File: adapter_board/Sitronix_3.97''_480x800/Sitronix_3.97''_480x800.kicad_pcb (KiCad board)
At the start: 2 copper layers, 32.5 x 54.9 mm, 6 parts, among them J1 ESP32-S3-LCD-EV-BOARD_SUB_LCD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, J2 Conn_02x26_Counter_Clockwise, J3 Conn_01x03, J4 Conn_01x02

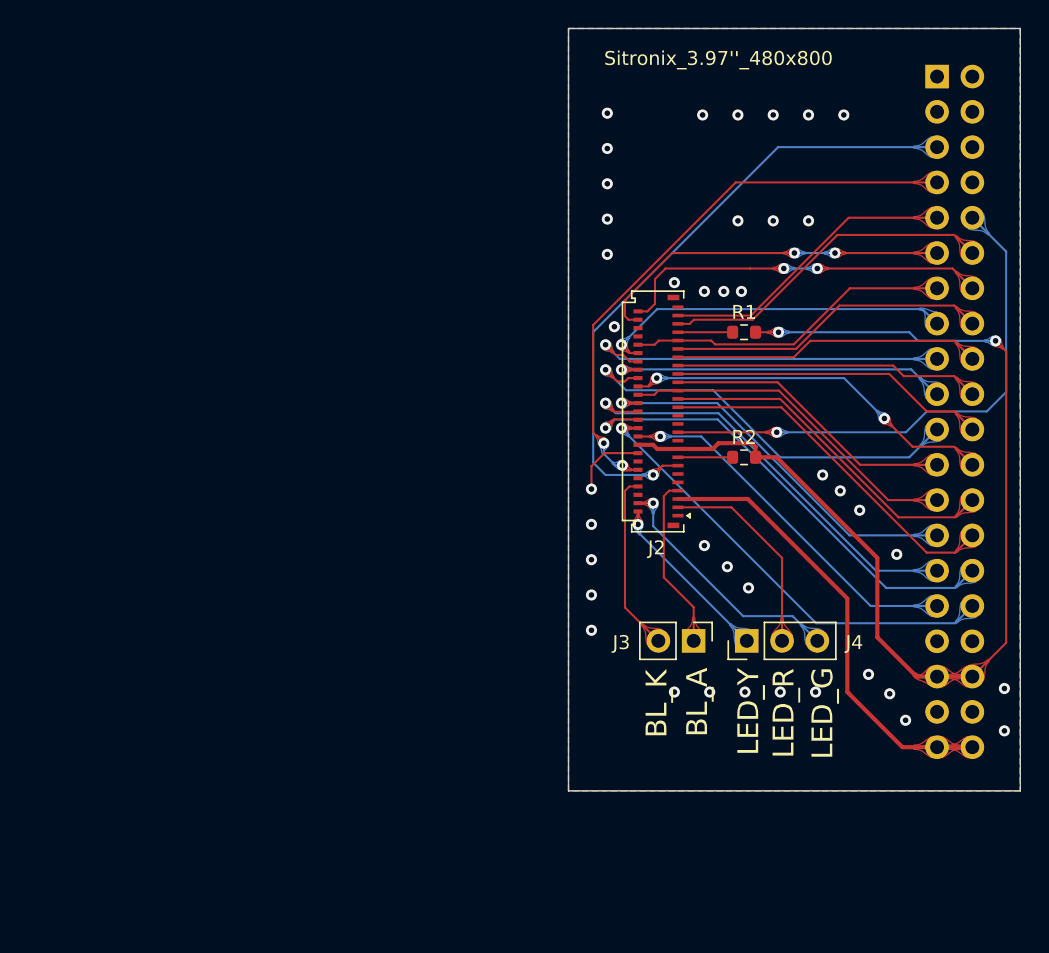
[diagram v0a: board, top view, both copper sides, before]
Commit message: adapter_board.sitronix_3.97''_800x480: modify
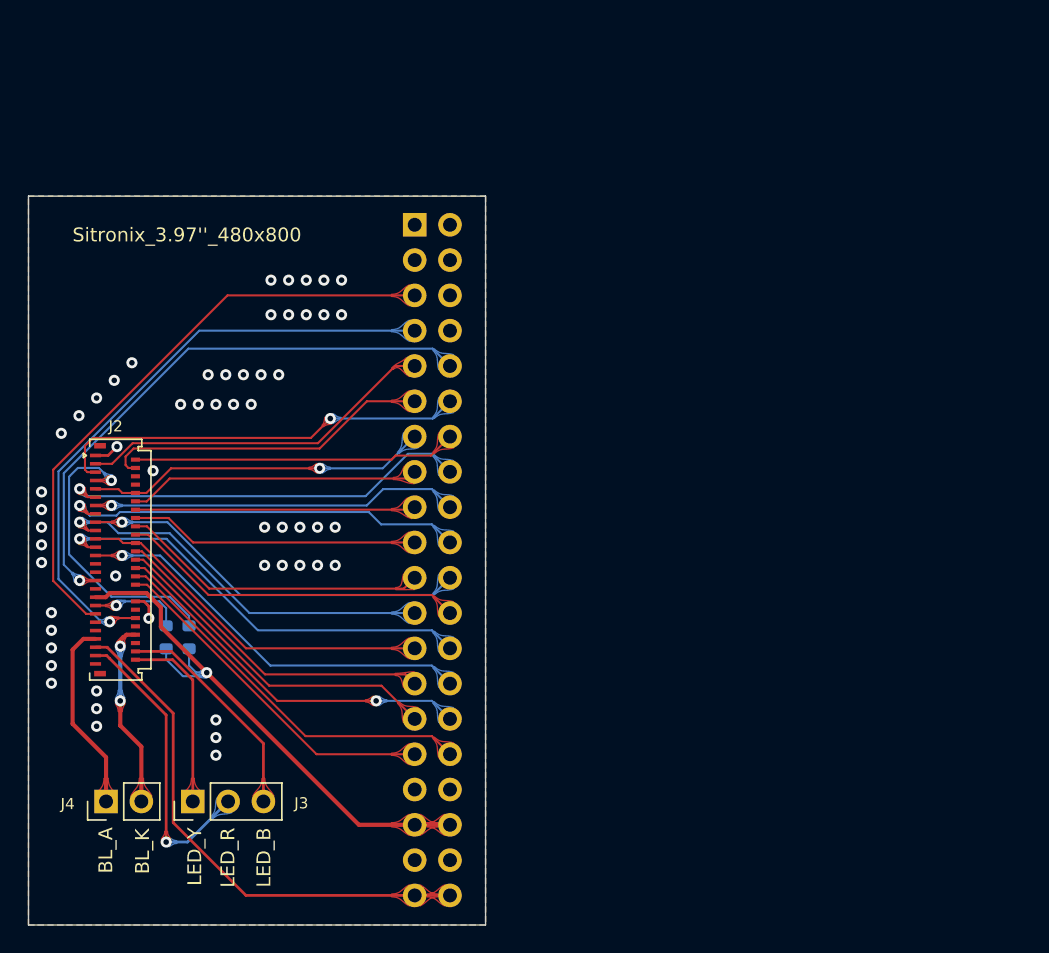
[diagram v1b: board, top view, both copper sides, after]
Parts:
- R1, R2: moved to B.Cu
- moved R1 45.6 mm to (46.7, 103.6), turned to -90 degrees
- moved J4 43.8 mm to (40.8, 115.4), turned to 90 degrees
- moved R2 43.6 mm to (45.1, 103.6), turned to -90 degrees
- moved J3 41.5 mm to (47.0, 115.4)
- moved J2 40.5 mm to (41.4, 98.0), turned to 0 degrees
- moved J1 39.1 mm to (63.0, 73.9)
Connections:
- J2 pad 10: unconnected-(J2-Pad10) -> /LCD_B3
- J2 pad 11: /GND -> /LCD_B4
- J2 pad 12: /TP_SCL -> /LCD_B5
- J2 pad 13: /TP_SDA -> /LCD_B6
- J2 pad 14: unconnected-(J2-Pad14) -> /LCD_B7
- J2 pad 15: Net-(J2-Pad15) -> /LCD_G2
- J2 pad 16: /GND -> /LCD_G3
- J2 pad 17: /VCC3.3V -> /LCD_G4
- J2 pad 18: /VCC3.3V -> /LCD_G5
- J2 pad 19: unconnected-(J2-Pad19) -> /LCD_G6
- J2 pad 2: /LCD_LED_Y -> /LCD_PCLK
- J2 pad 20: /SPI_CS -> /LCD_G7
- J2 pad 21: /SPI_DC -> /LCD_R3
- J2 pad 22: /SPI_SCK -> /LCD_R3
- J2 pad 23: unconnected-(J2-Pad23) -> /LCD_R4
- J2 pad 24: /SPI_MOSI -> /LCD_R5
- J2 pad 25: /GND -> /LCD_R6
- J2 pad 27: /LCD_R6 -> /GND
- J2 pad 28: /LCD_R5 -> /SPI_MOSI
- J2 pad 29: /LCD_R4 -> unconnected-(J2-Pad29)
- J2 pad 3: /LCD_LED_R -> /LCD_DE
- J2 pad 30: /LCD_R3 -> /SPI_SCK
- J2 pad 31: /LCD_R3 -> /SPI_DC
- J2 pad 32: /LCD_G7 -> /SPI_CS
- J2 pad 33: /LCD_G6 -> unconnected-(J2-Pad33)
- J2 pad 34: /LCD_G5 -> /VCC3.3V
- J2 pad 35: /LCD_G4 -> /VCC3.3V
- J2 pad 36: /LCD_G3 -> /GND
- J2 pad 37: /LCD_G2 -> Net-(J2-Pad37)
- J2 pad 38: /LCD_B7 -> unconnected-(J2-Pad38)
- J2 pad 39: /LCD_B6 -> /TP_SDA
- J2 pad 4: /LCD_LED_B -> /LCD_HSYNC
- J2 pad 40: /LCD_B5 -> /TP_SCL
- J2 pad 41: /LCD_B4 -> /GND
- J2 pad 42: /LCD_B3 -> unconnected-(J2-Pad42)
- J2 pad 43: /LCD_B3 -> /GND
- J2 pad 44: /GND -> /LCD_BL_K
- J2 pad 45: Net-(J2-Pad45) -> /LCD_BL_A
- J2 pad 46: /GND -> unconnected-(J2-Pad46)
- J2 pad 47: /LCD_VSYNC -> /VCC5V
- J2 pad 48: /LCD_HSYNC -> /LCD_LED_B
- J2 pad 49: /LCD_DE -> /LCD_LED_R
- J2 pad 5: /VCC5V -> /LCD_VSYNC
- J2 pad 50: /LCD_PCLK -> /LCD_LED_Y
- J2 pad 6: unconnected-(J2-Pad6) -> /GND
- J2 pad 7: /LCD_BL_A -> Net-(J2-Pad7)
- J2 pad 8: /LCD_BL_K -> /GND
- J2 pad 9: /GND -> /LCD_B3
- R1 pad 1: Net-(J2-Pad45) -> Net-(J2-Pad7)
- R2 pad 1: Net-(J2-Pad15) -> Net-(J2-Pad37)
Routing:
- net /VCC3.3V: track 78.1 -> 40.3 mm, vias 2 -> 1
- net Net-(J2-Pad7): track 0.00 -> 21.6 mm, vias 0 -> 1
- net /LCD_G5: track 30.1 -> 22.3 mm, vias 1 -> 0
- net /SPI_MOSI: track 34.8 -> 27.1 mm
- net /LCD_G2: track 22.0 -> 29.4 mm, vias 0 -> 1
- net /LCD_G6: track 21.1 -> 28.2 mm, vias 0 -> 1
- net /LCD_B4: track 23.0 -> 30.1 mm, vias 0 -> 1
- net /LCD_B7: track 27.1 -> 20.2 mm, vias 1 -> 0
- net /LCD_LED_R: track 15.0 -> 21.7 mm, vias 0 -> 1
- net Net-(J2-Pad37): track 0.00 -> 6.69 mm, vias 0 -> 1
- net /LCD_R7: track 31.5 -> 24.8 mm, vias 1 -> 0
- net /LCD_R4: track 25.2 -> 31.3 mm, vias 0 -> 1
- net /LCD_VSYNC: track 24.4 -> 30.1 mm, vias 0 -> 1
- net /LCD_G4: track 22.8 -> 28.2 mm, vias 0 -> 1
- net /VCC5V: track 32.5 -> 37.5 mm
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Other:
- board size 32.5 x 54.9 mm -> 32.9 x 52.5 mm
- board text added: "LED_B"
- board text removed: "LED_G"
